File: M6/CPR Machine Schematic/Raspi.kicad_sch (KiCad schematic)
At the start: 2 parts, among them J13 Raspberry_Pi_2_3

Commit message: Start of Board V2
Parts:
- added J15: Conn_02x20_Odd_Even, Connector_PinHeader_2.54mm:PinHeader_2x20_P2.54mm_Vertical, symbol Connector_Generic:Conn_02x20_Odd_Even
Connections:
- net +5V: now also J15.2 (Pin_2), J15.4 (Pin_4)
- net GND: now also J15.14 (Pin_14), J15.20 (Pin_20), J15.25 (Pin_25), J15.30 (Pin_30), J15.34 (Pin_34), J15.39 (Pin_39), J15.6 (Pin_6), J15.9 (Pin_9)
- net GPIO15: now reaches J13.10 (GPIO15/RXD)
- net GPIO15: now also J15.10 (Pin_10)
- net GPIO17: now reaches J13.11 (GPIO17)
- net GPIO17: now also J15.11 (Pin_11)
- net GPIO18: now reaches J13.12 (GPIO18/PWM0)
- net GPIO18: now also J15.12 (Pin_12)
- net GPIO27: now reaches J13.13 (GPIO27)
- net GPIO27: now also J15.13 (Pin_13)
- net GPIO22: now reaches J13.15 (GPIO22)
- net GPIO22: now also J15.15 (Pin_15)
- net GPIO10: now reaches J13.19 (MOSI0/GPIO10)
- net GPIO10: now also J15.19 (Pin_19)
- net GPIO9: now reaches J13.21 (MISO0/GPIO9)
- net GPIO9: now also J15.21 (Pin_21)
- net GPIO11: now reaches J13.23 (SCLK0/GPIO11)
- net GPIO11: now also J15.23 (Pin_23)
- net GPIO8: now reaches J13.24 (~{CE0}/GPIO8)
- net GPIO8: now also J15.24 (Pin_24)
- net GPIO7: now reaches J13.26 (~{CE1}/GPIO7)
- net GPIO7: now also J15.26 (Pin_26)
- net GPIO0: now reaches J13.27 (ID_SD/GPIO0)
- net GPIO0: now also J15.27 (Pin_27)
- net GPIO1: now reaches J13.28 (ID_SC/GPIO1)
- net GPIO1: now also J15.28 (Pin_28)
- net GPIO5: now reaches J13.29 (GCLK1/GPIO5)
- net GPIO5: now also J15.29 (Pin_29)
- net GPIO6: now reaches J13.31 (GCLK2/GPIO6)
- net GPIO6: now also J15.31 (Pin_31)
- net GPIO13: now reaches J13.33 (PWM1/GPIO13)
- net GPIO13: now also J15.33 (Pin_33)
- net GPIO19: now reaches J13.35 (GPIO19/MISO1)
- net GPIO19: now also J15.35 (Pin_35)
- net GPIO16: now reaches J13.36 (GPIO16)
- net GPIO16: now also J15.36 (Pin_36)
- net GPIO20: now reaches J13.38 (GPIO20/MOSI1)
- net GPIO20: now also J15.38 (Pin_38)
- net GPIO21: now reaches J13.40 (GPIO21/SCLK1)
- net GPIO21: now also J15.40 (Pin_40)
- net GPIO4: now reaches J13.7 (GCLK0/GPIO4)
- net GPIO4: now also J15.7 (Pin_7)
- net GPIO14: now reaches J13.8 (GPIO14/TXD)
- net GPIO14: now also J15.8 (Pin_8)
- new net +3.3V: J15.1 (Pin_1), J15.17 (Pin_17)
- no-connect marks 23 -> 9
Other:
- note added: "Spare GPIO Header"

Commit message: Board V2 Final
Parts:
- F2, J13, J15: now left out of the parts list
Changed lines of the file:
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@@
 		(unit 1)
 		(exclude_from_sim no)
-		(in_bom yes)
+		(in_bom no)
 		(on_board yes)
 		(dnp no)
@@
 			)
 		)
+		(property "Notes" ""
+			(at 140.97 110.49 0)
+			(effects
+				(font
+					(size 1.27 1.27)
+				)
+				(hide yes)
+			)
+		)
 		(pin "36"
 		)
@@
 		(unit 1)
 		(exclude_from_sim no)
-		(in_bom yes)
+		(in_bom no)
 		(on_board yes)
 		(dnp no)
@@
 			)
 		)
+		(property "Notes" ""
+			(at 135.89 72.39 0)
+			(effects
+				(font
+					(size 1.27 1.27)
+				)
+				(hide yes)
+			)
+		)
 		(pin "2"
 		)
@@
 		(unit 1)
 		(exclude_from_sim no)
-		(in_bom yes)
+		(in_bom no)
 		(on_board yes)
 		(dnp no)
@@
 			(at 203.2 109.22 0)
 			(effects
+				(font
+					(size 1.27 1.27)
+				)
+				(hide yes)
+			)
+		)
+		(property "Notes" ""
+			(at 203.2 109.22 0)
+			(effects

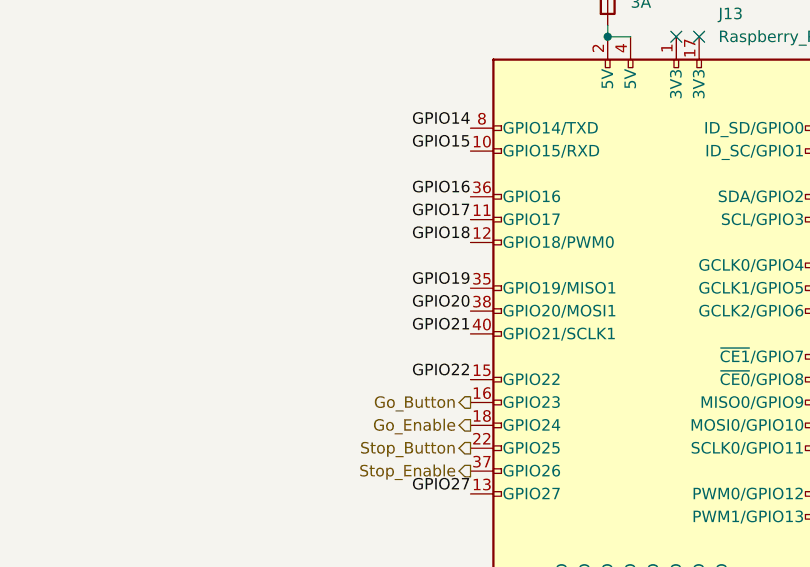
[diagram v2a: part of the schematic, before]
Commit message: Voltage readout, MUX, Debouncing Caps
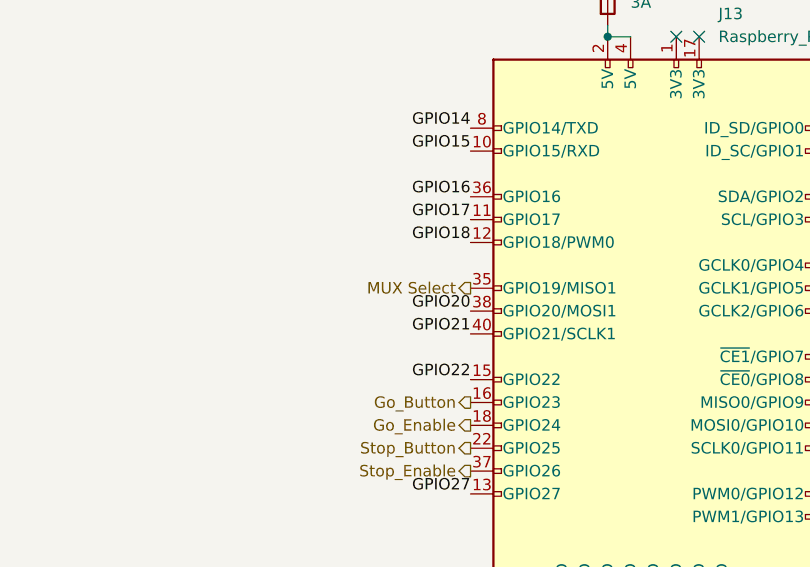
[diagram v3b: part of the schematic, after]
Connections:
- net GPIO19: no longer J13.35 (GPIO19/MISO1)
- new net MUX Select: J13.35 (GPIO19/MISO1)
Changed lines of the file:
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@@
-		)
-	)
-	(label "GPIO19"
-		(at 120.65 105.41 180)
-		(effects
-			(font
-				(size 1.27 1.27)
-			)
-			(justify right bottom)
 		)
 	)
@@
 		(effects
 			(font
+				(size 1.27 1.27)
+			)
+			(justify right)
+		)
+	)
+	(hierarchical_label "MUX Select"
+		(shape output)
+		(at 120.65 105.41 180)
+		(effects
+			(font
